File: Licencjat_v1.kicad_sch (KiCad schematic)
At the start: 67 parts, among them J1 PV_IN_1, J2 PV_IN_2, J3 AHT20 + BMP280, J4 VEML7700, J5 ADDITIONAL I2C, J6 RF_TRANSMITTER, J7 AVR-ISP-6, J8 GEIGER, J9 1_WIRE, Q1 AO3401A, Q10 2SC1945, Q11 AO3400A, Q2 BC846, Q3 AO3401A, Q4 AO3400A, Q5 AO3400A, Q6 AO3400A, Q7 AO3401A, Q8 AO3401A, Q9 2SC1945, U1 ATmega328P-A, U2 XC6206PxxxMR, U3 HT75xx-1-SOT89, Y1 Crystal_Small

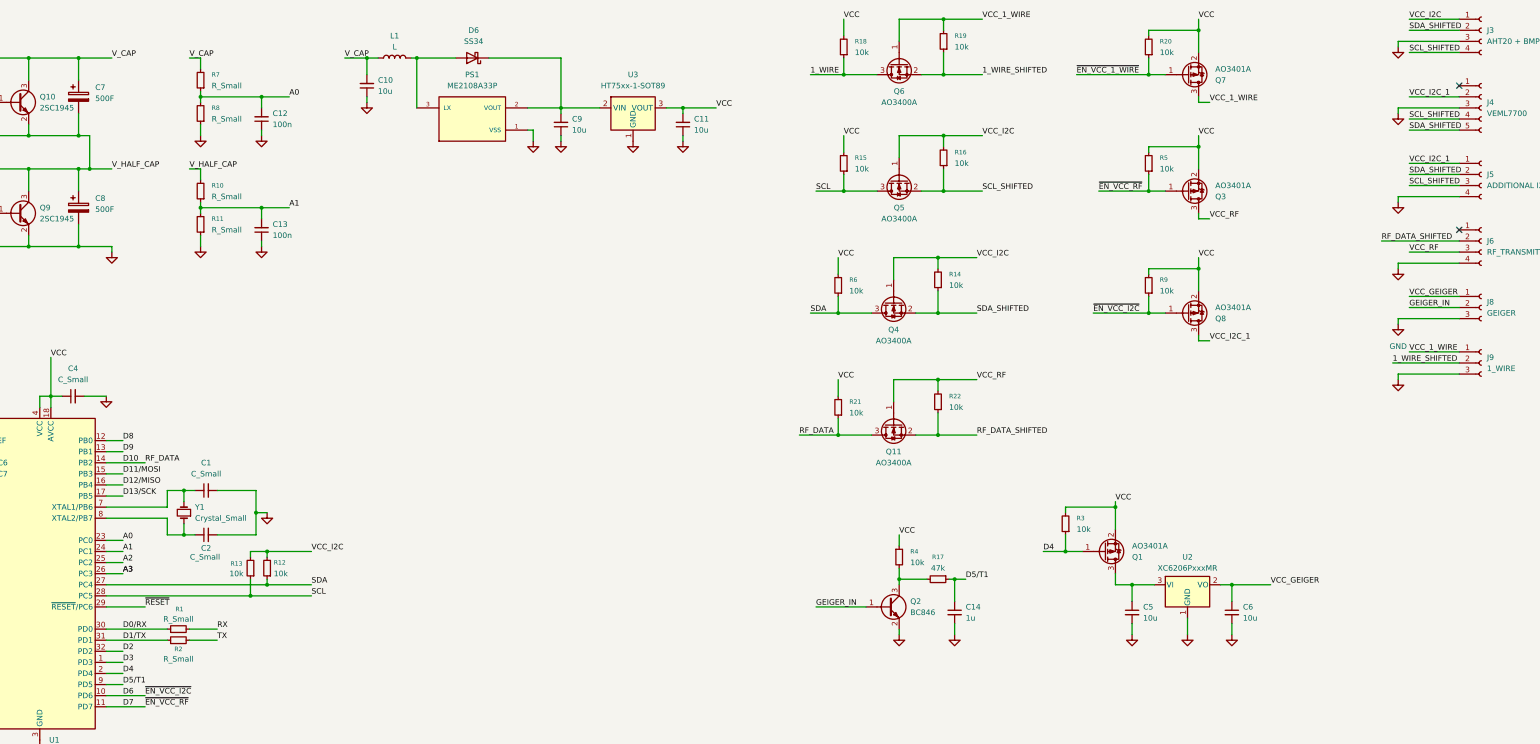
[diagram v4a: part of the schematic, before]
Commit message: Component placing continues
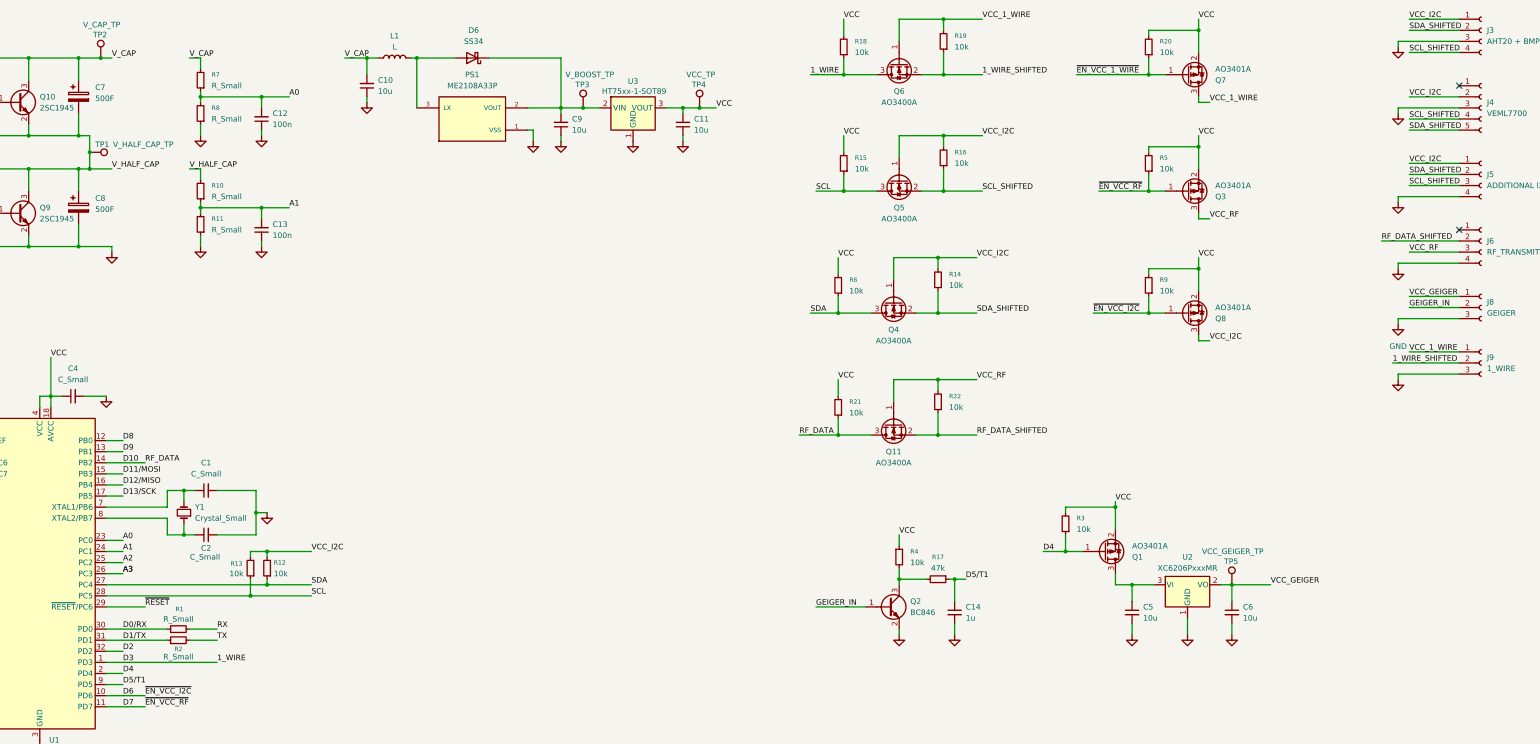
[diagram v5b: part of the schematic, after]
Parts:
- added TP1: V_HALF_CAP_TP, TestPoint:TestPoint_Pad_D2.0mm, symbol Connector:TestPoint
- added TP2: V_CAP_TP, TestPoint:TestPoint_Pad_D2.0mm, symbol Connector:TestPoint
- added TP3: V_BOOST_TP, TestPoint:TestPoint_Pad_D2.0mm, symbol Connector:TestPoint
- added TP4: VCC_TP, TestPoint:TestPoint_Pad_D2.0mm, symbol Connector:TestPoint
- added TP5: VCC_GEIGER_TP, TestPoint:TestPoint_Pad_D2.0mm, symbol Connector:TestPoint
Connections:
- net D3 is gone; now on net 1_WIRE: U1.1 (PD3)
- net VCC_I2C_1 is gone; now on net VCC_I2C: J4.2 (Pin_2), J5.1 (Pin_1), Q8.3 (D)
- net GND: now also C12.1, R8.1
- net VCC: now also TP4.1
- net VCC_GEIGER: now also TP5.1
- net V_CAP: now also TP2.1
- net V_HALF_CAP: now also TP1.1
- net at C9.2, D6.1 (K), PS1.2 (VOUT)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: now also TP3.1

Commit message: Elements placed
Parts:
- removed R12, R13: 10k, Resistor_SMD:R_1206_3216Metric, symbol Device:R_Small
- added J10: SERIAL, Connector_PinHeader_2.54mm:PinHeader_1x04_P2.54mm_Vertical, symbol Connector:Conn_01x04_Socket
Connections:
- net A0: now also C13.2, R10.1, R11.2; no longer C12.2, R7.1, R8.2
- net A1: now also C12.2, R7.1, R8.2; no longer C13.2, R10.1, R11.2
- net GND: now also J10.4 (Pin_4)
- net RX: now also J10.3 (Pin_3)
- net TX: now also J10.2 (Pin_2)
- net VCC: now also J10.1 (Pin_1)

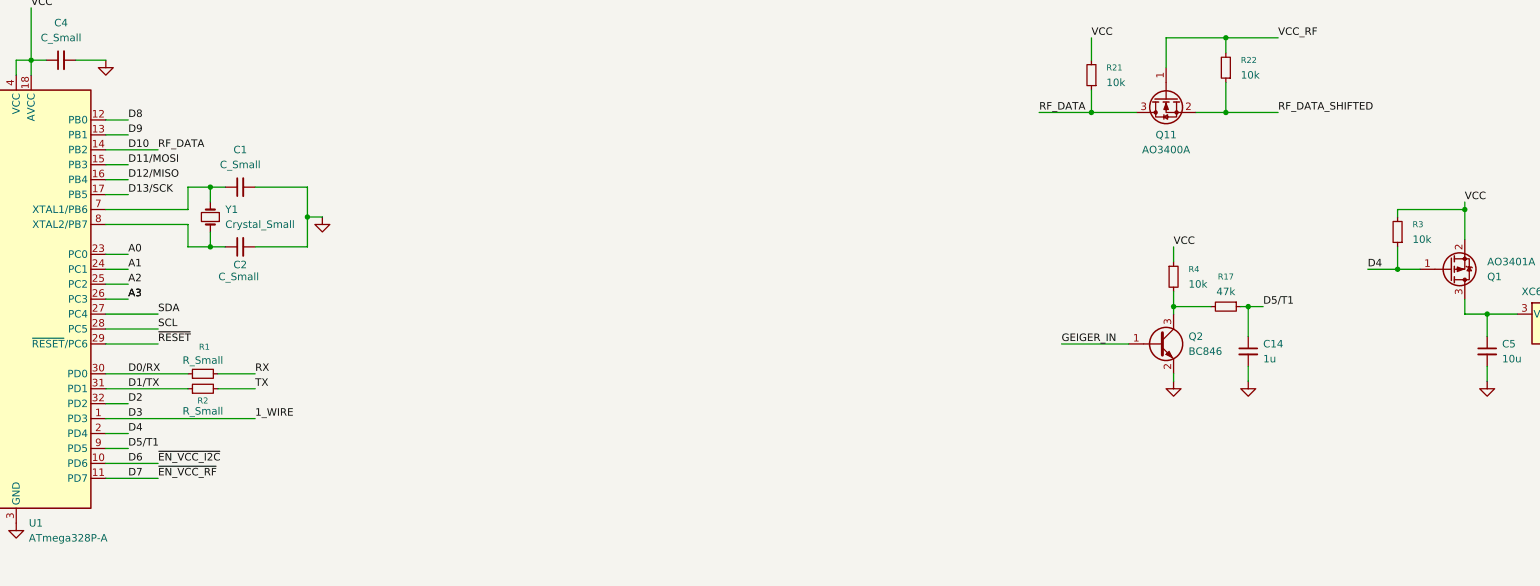
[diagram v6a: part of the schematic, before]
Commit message: Tracks placed
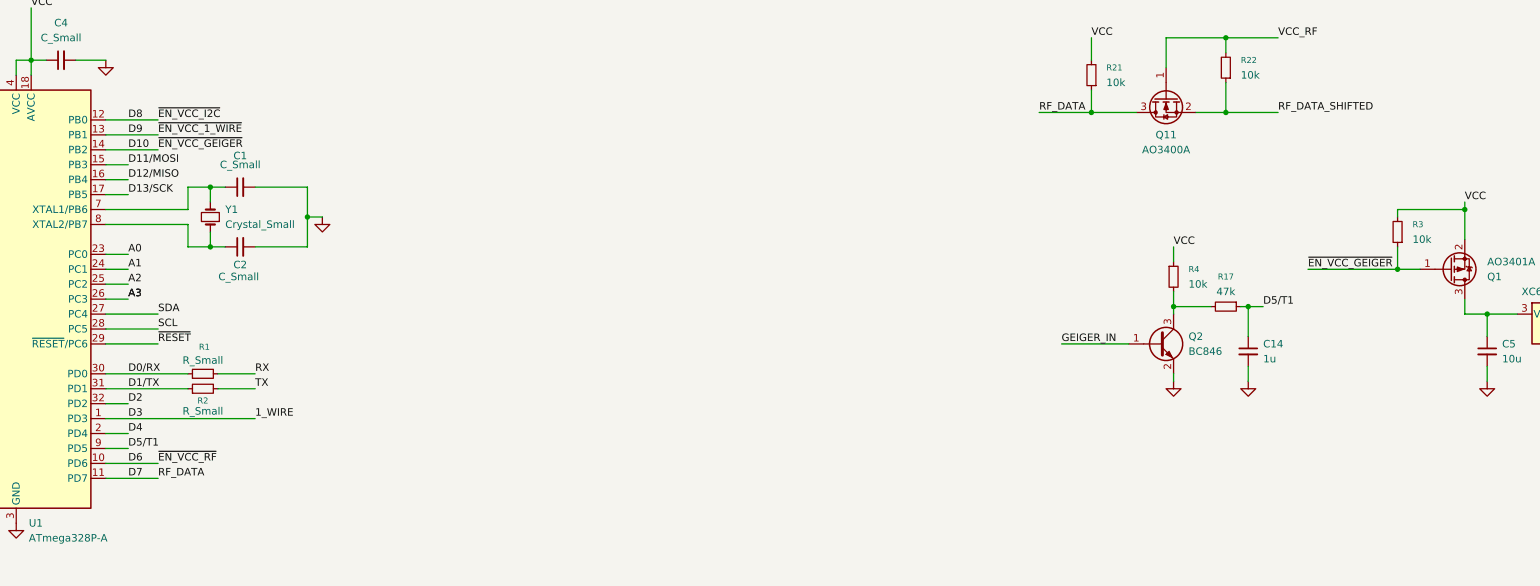
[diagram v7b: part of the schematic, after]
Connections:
- net ~{EN_VCC_1_WIRE} is gone; now on net D9: Q7.1 (G), R20.1
- net D10: now also Q1.1 (G), R3.1; no longer Q11.3 (D), R21.1
- net D4: no longer Q1.1 (G), R3.1
- net D6: now also Q3.1 (G), R5.1; no longer Q8.1 (G), R9.1
- net D7: now also Q11.3 (D), R21.1; no longer Q3.1 (G), R5.1
- net D8: now also Q8.1 (G), R9.1
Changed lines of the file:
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@@
 	(wire
 		(pts
-			(xy 71.12 118.11) (xy 74.93 118.11)
+			(xy 71.12 118.11) (xy 80.01 118.11)
 		)
 		(stroke
@@
 	(wire
 		(pts
-			(xy 285.75 143.51) (xy 290.83 143.51)
+			(xy 275.59 143.51) (xy 290.83 143.51)
 		)
 		(stroke
@@
 	(wire
 		(pts
-			(xy 71.12 120.65) (xy 74.93 120.65)
+			(xy 71.12 120.65) (xy 80.01 120.65)
 		)
 		(stroke
@@
 		)
 	)
-	(label "RF_DATA"
-		(at 80.01 123.19 0)
-		(effects
-			(font
-				(size 1.27 1.27)
-			)
-			(justify left bottom)
-		)
-	)
 	(label "D10"
 		(at 74.93 123.19 0)
@@
 		)
 	)
+	(label "~{EN_VCC_RF}"
+		(at 80.01 176.53 0)
+		(effects
+			(font
+				(size 1.27 1.27)
+			)
+			(justify left bottom)
+		)
+	)
 	(label "VCC"
 		(at 238.76 76.2 0)
@@
 		)
 	)
+	(label "~{EN_VCC_I2C}"
+		(at 80.01 118.11 0)
+		(effects
+			(font
+				(size 1.27 1.27)
+			)
+			(justify left bottom)
+		)
+	)
 	(label "SCL_SHIFTED"
 		(at 369.57 59.69 0)
@@
 		)
 	)
-	(label "~{EN_VCC_RF}"
-		(at 80.01 179.07 0)
-		(effects
-			(font
-				(size 1.27 1.27)
-			)
-			(justify left bottom)
-		)
-	)
 	(label "~{EN_VCC_1_WIRE}"
 		(at 293.37 34.29 0)
@@
 		)
 	)
+	(label "~{EN_VCC_GEIGER}"
+		(at 80.01 123.19 0)
+		(effects
+			(font
+				(size 1.27 1.27)
+			)
+			(justify left bottom)
+		)
+	)
 	(label "VCC_1_WIRE"
 		(at 271.78 21.59 0)
@@
 		)
 	)
+	(label "RF_DATA"
+		(at 80.01 179.07 0)
+		(effects
+			(font
+				(size 1.27 1.27)
+			)
+			(justify left bottom)
+		)
+	)
 	(label "SCL_SHIFTED"
 		(at 369.57 29.21 0)
@@
 		)
 	)
+	(label "~{EN_VCC_1_WIRE}"
+		(at 80.01 120.65 0)
+		(effects
+			(font
+				(size 1.27 1.27)
+			)
+			(justify left bottom)
+		)
+	)
 	(label "VCC"
 		(at 44.45 213.36 0)
@@
 		)
 	)
-	(label "~{EN_VCC_I2C}"
-		(at 80.01 176.53 0)
-		(effects
-			(font
-				(size 1.27 1.27)
-			)
-			(justify left bottom)
-		)
-	)
 	(label "SDA_SHIFTED"
 		(at 369.57 57.15 0)
@@
 		)
 	)
-	(label "D4"
-		(at 285.75 143.51 0)
+	(label "~{EN_VCC_GEIGER}"
+		(at 275.59 143.51 0)
 		(effects
 			(font
@@
 		(on_board yes)
 		(dnp no)
-		(fields_autoplaced yes)
 		(property "Reference" "C1"
-			(at 93.9863 123.19 90)
+			(at 93.98 124.206 90)
 			(effects
 				(font

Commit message: Adjust values
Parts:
- C1, C2: value C_Small -> 22p
- C14: value 1u -> 100p
- C3: value C_Small -> 100n
- C4: value C_Small -> 10u
- L1: value L -> 10u
- Q10, Q9: value 2SC1945 -> D880
- Q11, Q4, Q5, Q6: value AO3400A -> BSS138
- Q2: value BC846 -> BC847
- R1, R2: value R_Small -> 1k
- R10, R7: value R_Small -> 100k
- R11, R8: value R_Small -> 1M
- R17: value 47k -> 470k
- R20, R3, R5, R9: value 10k -> 1M
- R4: value 10k -> 240k
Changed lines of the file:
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@@
 			)
 		)
-		(property "Value" "47k"
+		(property "Value" "470k"
 			(at 261.62 147.32 90)
 			(effects
@@
 			)
 		)
-		(property "Value" "R_Small"
+		(property "Value" "1M"
 			(at 95.25 69.8499 0)
 			(effects
@@
 			)
 		)
-		(property "Value" "R_Small"
+		(property "Value" "100k"
 			(at 95.25 62.2299 0)
 			(effects
@@
 			)
 		)
-		(property "Value" "R_Small"
+		(property "Value" "1k"
 			(at 87.63 159.004 90)
 			(effects
@@
 			)
 		)
-		(property "Value" "C_Small"
-			(at 93.726 144.78 90)
+		(property "Value" "22p"
+			(at 94.234 144.78 90)
 			(effects
 				(font
@@
 			)
 		)
-		(property "Value" "C_Small"
+		(property "Value" "10u"
 			(at 63.5063 104.14 90)
 			(effects
@@
 			)
 		)
-		(property "Value" "10k"
+		(property "Value" "1M"
 			(at 293.37 138.4299 0)
 			(effects
@@
 			)
 		)
-		(property "Value" "AO3400A"
+		(property "Value" "BSS138"
 			(at 251.46 95.25 90)
 			(effects
@@
 			)
 		)
-		(property "Value" "2SC1945"
+		(property "Value" "D880"
 			(at 55.88 41.9099 0)
 			(effects
@@
 			)
 		)
-		(property "Value" "R_Small"
+		(property "Value" "100k"
 			(at 95.25 36.8299 0)
 			(effects
@@
 			)
 		)
-		(property "Value" "10k"
+		(property "Value" "1M"
 			(at 312.42 83.8199 0)
 			(effects
@@
 			)
 		)
-		(property "Value" "2SC1945"
+		(property "Value" "D880"
 			(at 55.88 67.3099 0)
 			(effects
@@
 			)
 		)
-		(property "Value" "C_Small"
-			(at 93.9863 125.73 90)
+		(property "Value" "22p"
+			(at 93.98 126.238 90)
 			(effects
 				(font
@@
 			)
 		)
-		(property "Value" "BC846"
+		(property "Value" "BC847"
 			(at 255.27 157.4799 0)
 			(effects
@@
 			)
 		)
-		(property "Value" "10k"
+		(property "Value" "1M"
 			(at 312.42 29.2099 0)
 			(effects
@@
 			)
 		)
-		(property "Value" "10k"
+		(property "Value" "1M"
 			(at 312.42 55.8799 0)
 			(effects
@@
 		(on_board yes)
 		(dnp no)
-		(fields_autoplaced yes)
 		(property "Reference" "R4"
-			(at 255.27 143.5099 0)
+			(at 255.778 141.732 0)
 			(effects
 				(font
@@
 			)
 		)
-		(property "Value" "10k"
-			(at 255.27 146.0499 0)
+		(property "Value" "240k"
+			(at 254.508 144.018 0)
 			(effects
 				(font
@@
 			)
 		)
-		(property "Value" "1u"
+		(property "Value" "100p"
 			(at 267.97 158.7562 0)
 			(effects
@@
 			)
 		)
-		(property "Value" "C_Small"
+		(property "Value" "100n"
 			(at 34.2963 114.3 90)
 			(effects
@@
 			)
 		)
-		(property "Value" "AO3400A"
+		(property "Value" "BSS138"
 			(at 252.73 40.64 90)
 			(effects
@@
 			)
 		)
-		(property "Value" "R_Small"
+		(property "Value" "1M"
 			(at 95.25 44.4499 0)
 			(effects
@@
 			)
 		)
-		(property "Value" "L"
+		(property "Value" "10u"
 			(at 137.16 27.94 90)
 			(effects
@@
 			)
 		)
-		(property "Value" "AO3400A"
+		(property "Value" "BSS138"
 			(at 252.73 67.31 90)
 			(effects
@@
 			)
 		)
-		(property "Value" "AO3400A"
+		(property "Value" "BSS138"
 			(at 251.46 123.19 90)
 			(effects
@@
 			)
 		)
-		(property "Value" "R_Small"
+		(property "Value" "1k"
 			(at 87.63 167.64 90)
 			(effects
